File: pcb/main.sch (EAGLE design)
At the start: 45 parts, among them IC1 FT230XS, J3 455-1750-1-ND, J6 M1 connector, J7 M2 connector, Q1 2.5A/30V/105mΩ, U1 LSM303C, U2 ESP-WROOM-32

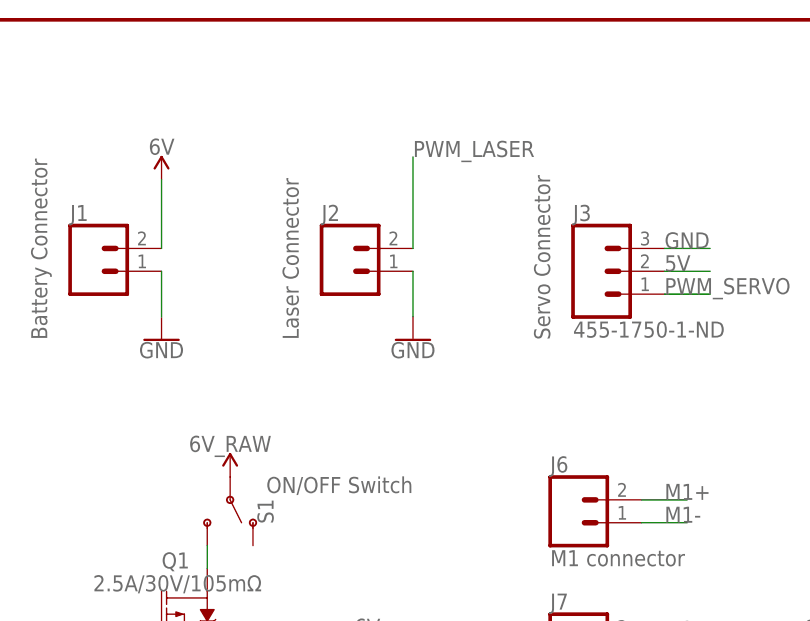
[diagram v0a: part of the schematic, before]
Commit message: mosfet for laser
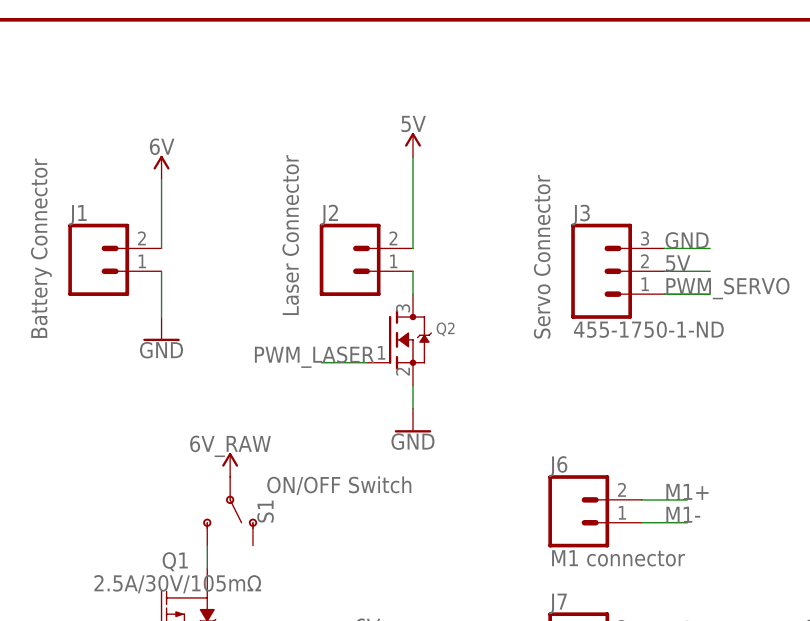
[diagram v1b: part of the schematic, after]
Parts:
- added Q2: (no value), adafruit:MOSFET-NREFLOW
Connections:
- new net N$10: J2.1, Q2.D
- net 5V: now also J2.2
- net GND: now also Q2.S; no longer J2.1
- net PWM_LASER: now also Q2.G; no longer J2.2
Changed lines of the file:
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@@
 <part name="SUPPLY14" library="SparkFun-PowerSymbols" deviceset="VCC" device="" value="3V3"/>
 <part name="RESET" library="DiscreteComponents" deviceset="SWITCH" device="" value=""/>
+<part name="Q2" library="adafruit" library_urn="urn:adsk.eagle:library:420" deviceset="MOSFET-N" device="REFLOW"/>
+<part name="SUPPLY15" library="SparkFun-PowerSymbols" deviceset="VCC" device="" value="5V"/>
 </parts>
 <sheets>
@@
 </instance>
 <instance part="J2" gate="G$1" x="45.72" y="157.48">
-<attribute name="COMM" x="40.64" y="149.86" size="1.778" layer="96" rot="R90"/>
+<attribute name="COMM" x="40.64" y="152.4" size="1.778" layer="96" rot="R90"/>
 </instance>
 <instance part="J3" gate="J$1" x="73.66" y="157.48">
@@
 <instance part="GND1" gate="1" x="142.24" y="152.4"/>
 <instance part="GND2" gate="1" x="116.84" y="152.4"/>
-<instance part="GND3" gate="1" x="53.34" y="149.86"/>
+<instance part="GND3" gate="1" x="53.34" y="139.7"/>
 <instance part="GND4" gate="1" x="25.4" y="149.86"/>
 <instance part="GND5" gate="1" x="38.1" y="45.72"/>
@@
 <instance part="SUPPLY14" gate="G$1" x="172.72" y="124.46"/>
 <instance part="RESET" gate="G$1" x="228.6" y="129.54"/>
+<instance part="Q2" gate="G$1" x="50.8" y="149.86"/>
+<instance part="SUPPLY15" gate="G$1" x="53.34" y="170.18"/>
 </instances>
 <busses>
@@
 <net name="PWM_LASER" class="0">
 <segment>
-<pinref part="J2" gate="G$1" pin="2"/>
-<wire x1="53.34" y1="160.02" x2="53.34" y2="170.18" width="0.1524" layer="91"/>
-<label x="53.34" y="170.18" size="1.778" layer="95"/>
+<pinref part="Q2" gate="G$1" pin="G"/>
+<wire x1="48.26" y1="147.32" x2="43.18" y2="147.32" width="0.1524" layer="91"/>
+<label x="35.56" y="147.32" size="1.778" layer="95"/>
 </segment>
 </net>
@@
 <wire x1="25.4" y1="157.48" x2="25.4" y2="152.4" width="0.1524" layer="91"/>
 <pinref part="GND4" gate="1" pin="GND"/>
-</segment>
-<segment>
-<wire x1="53.34" y1="157.48" x2="53.34" y2="152.4" width="0.1524" layer="91"/>
-<pinref part="J2" gate="G$1" pin="1"/>
-<pinref part="GND3" gate="1" pin="GND"/>
 </segment>
 <segment>
@@
 <pinref part="GND18" gate="1" pin="GND"/>
 </segment>
+<segment>
+<pinref part="Q2" gate="G$1" pin="S"/>
+<pinref part="GND3" gate="1" pin="GND"/>
+<wire x1="53.34" y1="144.78" x2="53.34" y2="142.24" width="0.1524" layer="91"/>
+</segment>
 </net>
 <net name="5V" class="0">
@@
 <junction x="55.88" y="63.5"/>
 <pinref part="U$1" gate="G$1" pin="OUTPUT"/>
+</segment>
+<segment>
+<pinref part="J2" gate="G$1" pin="2"/>
+<wire x1="53.34" y1="160.02" x2="53.34" y2="170.18" width="0.1524" layer="91"/>
+<pinref part="SUPPLY15" gate="G$1" pin="VCC"/>
 </segment>
 </net>
@@
 </segment>
 </net>
+<net name="N$10" class="0">
+<segment>
+<pinref part="Q2" gate="G$1" pin="D"/>
+<pinref part="J2" gate="G$1" pin="1"/>
+<wire x1="53.34" y1="154.94" x2="53.34" y2="157.48" width="0.1524" layer="91"/>
+</segment>
+</net>

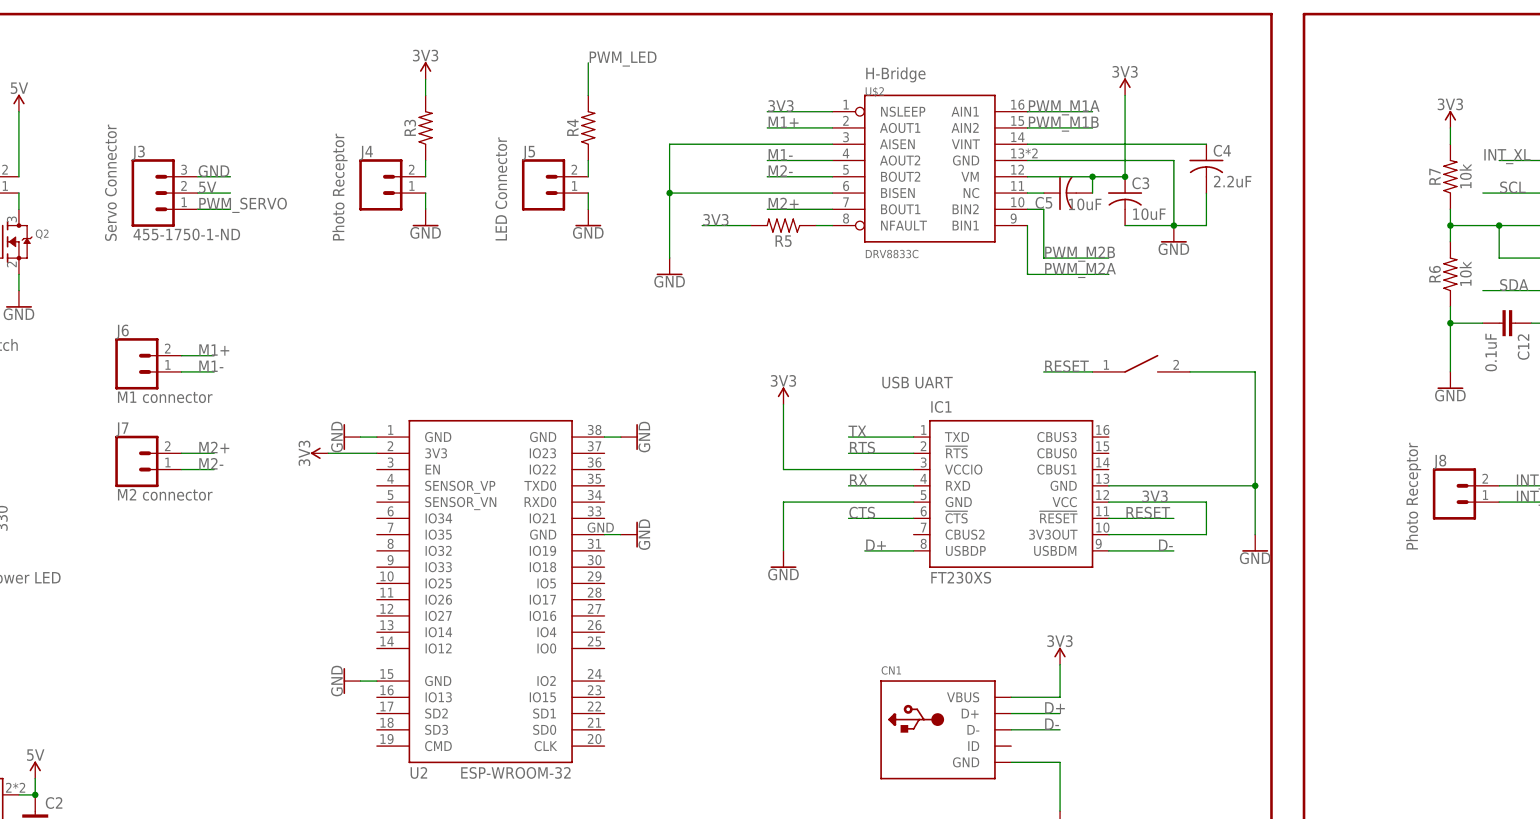
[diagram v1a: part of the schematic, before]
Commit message: wired up almost all of esp's peripherals
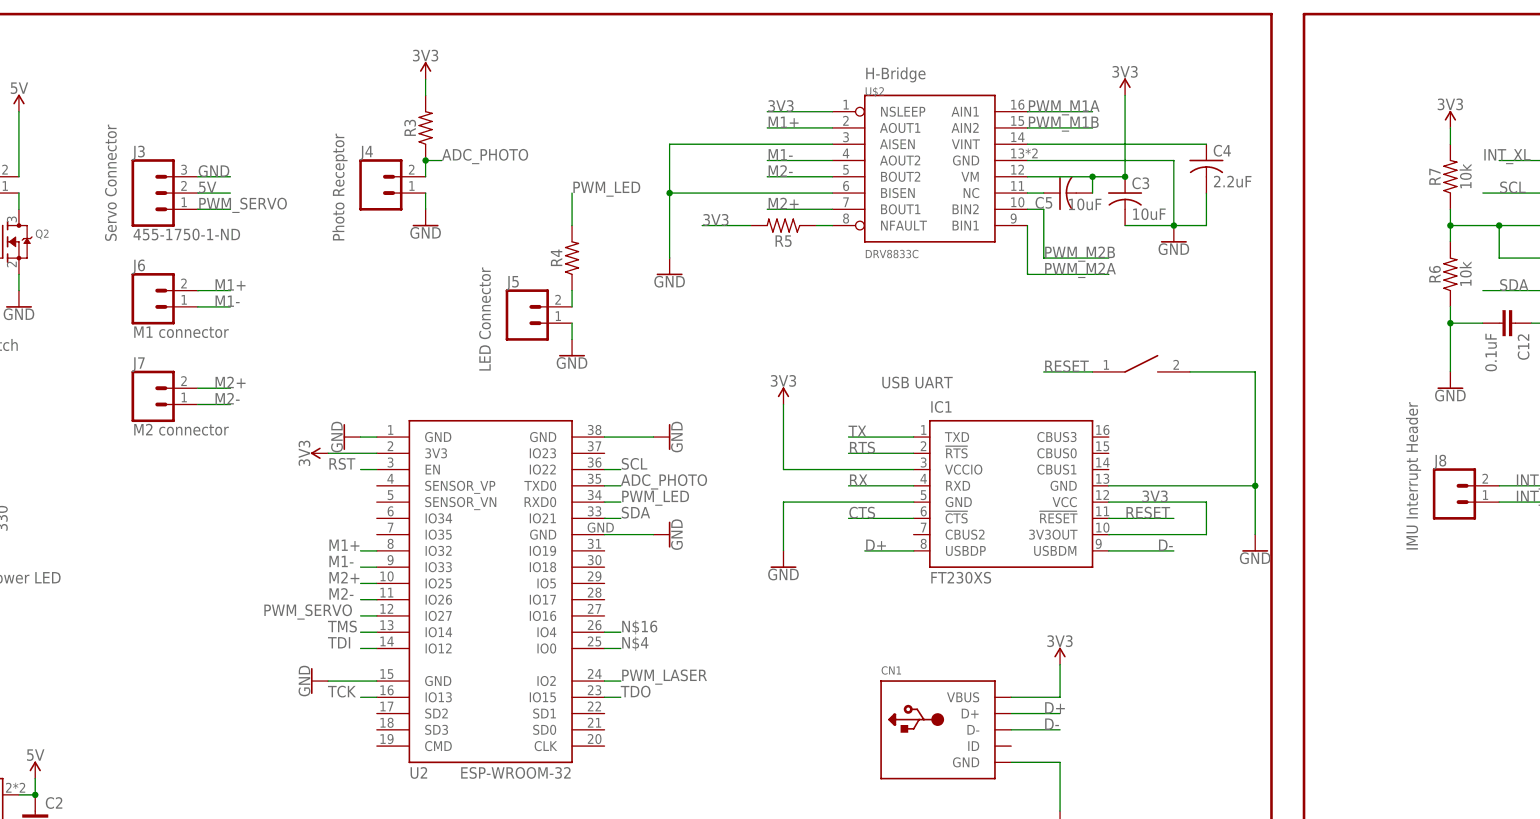
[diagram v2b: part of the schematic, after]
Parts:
- J8: COMM Photo Receptor -> IMU Interrupt Header
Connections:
- new net ADC_PHOTO: J4.2, R3.1, U2.TXD0
- new net N$16: U2.IO4
- new net RST: U2.EN
- new net TCK: U2.IO13
- new net TDI: U2.IO12
- new net TDO: U2.IO15
- new net TMS: U2.IO14
- net M1+: now also U2.IO32
- net M1-: now also U2.IO33
- net M2+: now also U2.IO25
- net M2-: now also U2.IO26
- net N$4: now also U2.IO0; no longer J4.2, R3.1
- net PWM_LASER: now also U2.IO2
- net PWM_LED: now also U2.RXD0
- net PWM_SERVO: now also U2.IO27
- net SCL: now also U2.IO22
- net SDA: now also U2.IO21
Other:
- moved on the sheet: J5, J6, J7, R4

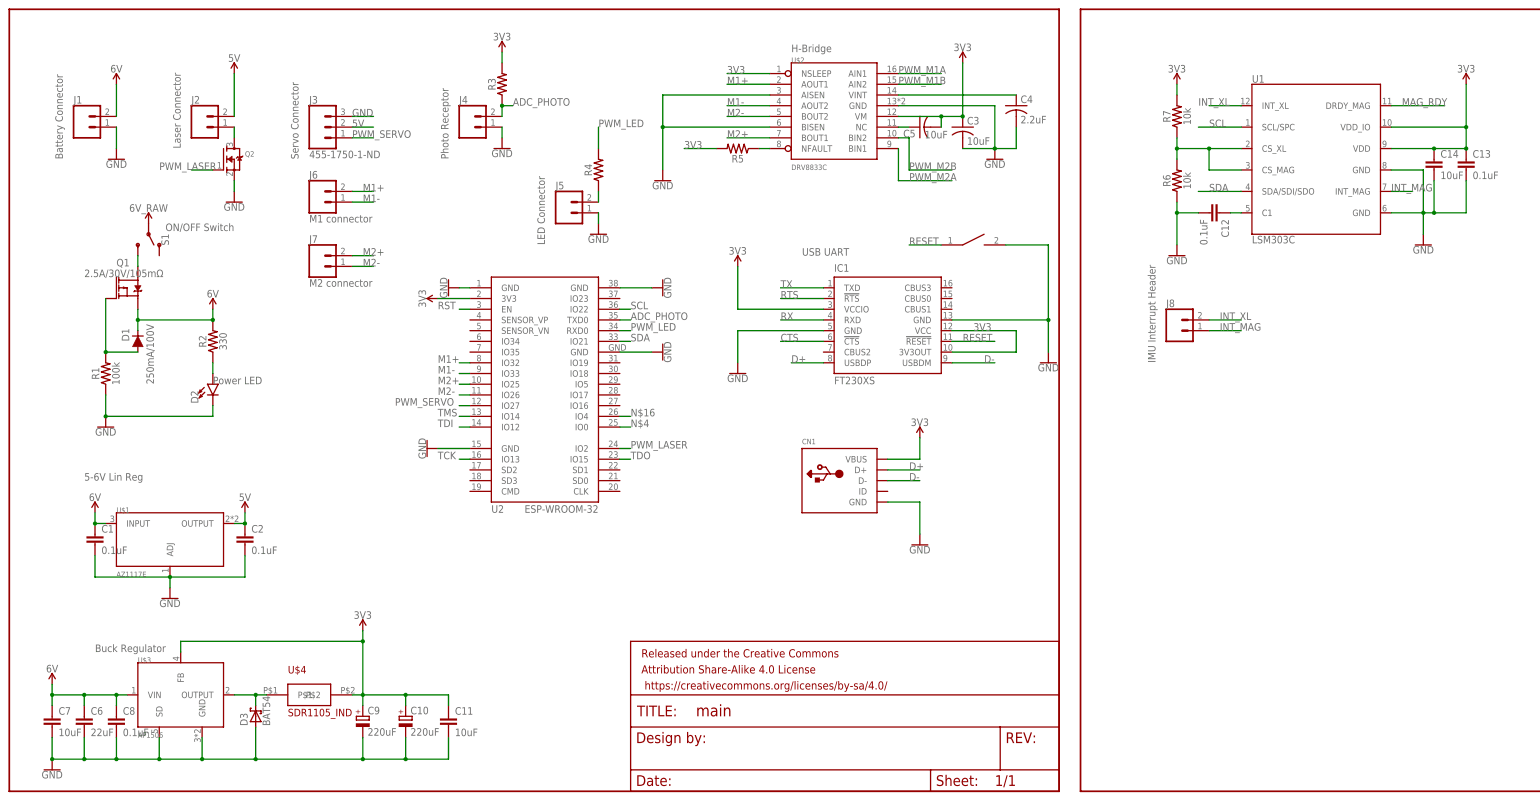
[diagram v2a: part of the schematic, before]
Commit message: more esp pins and isolating grounds
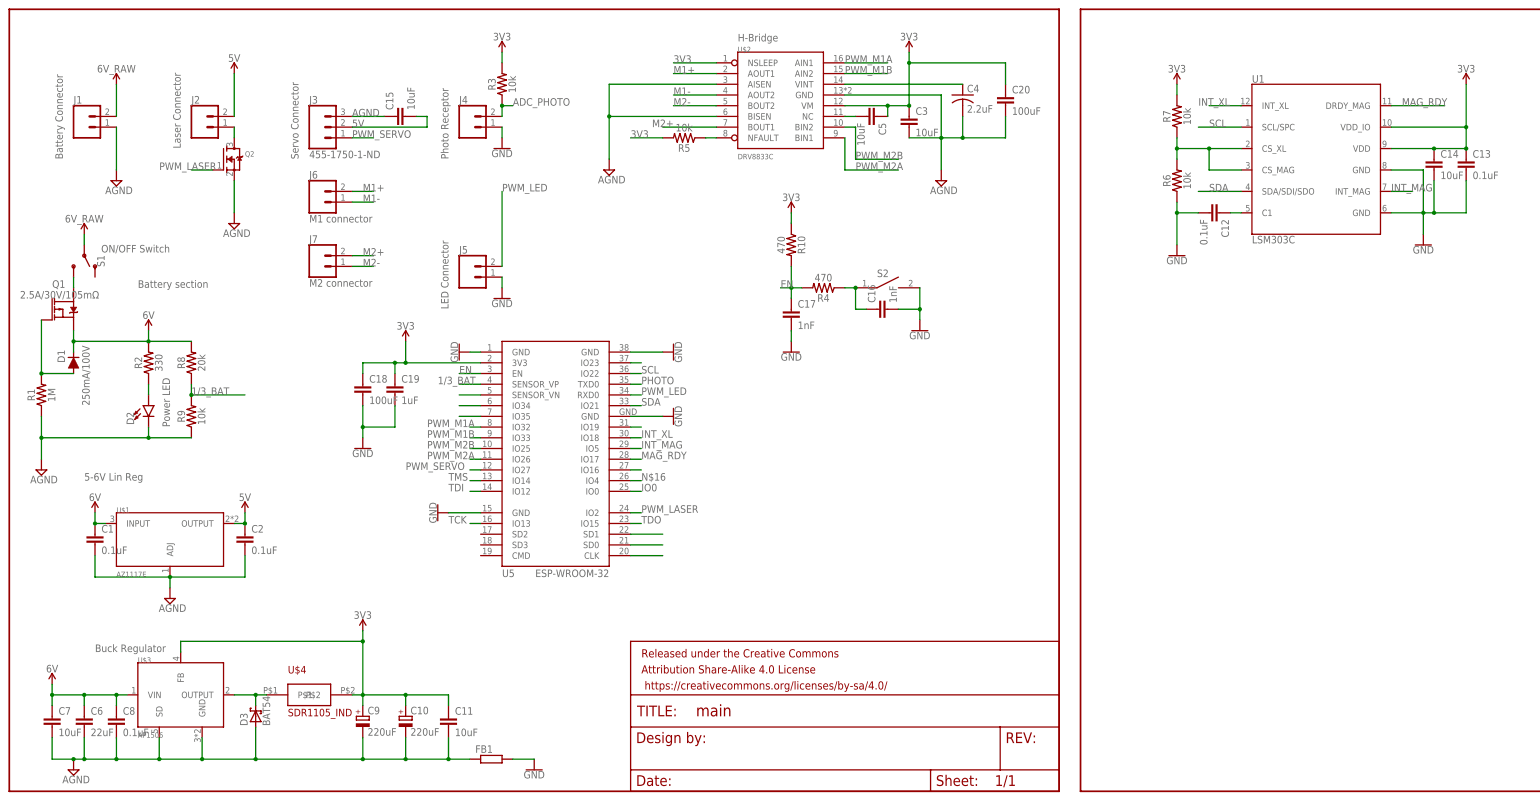
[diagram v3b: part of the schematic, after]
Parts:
- removed CN1: (no value), adafruit:USBMINIB
- removed IC1: FT230XS, electricSheepParty:FT230XS
- removed J8: (no value), electricSheepParty:CONN_02
- removed RESET: SWITCH, DiscreteComponents:SWITCH
- removed U2: ESP-WROOM-32, electricSheepParty:ESP-WROOM-32
- added C15: 10uF, rcl:C-EUC0805
- added C16, C17: 1nF, electricSheepParty:0.1UF-0603-25V-(+80/-20%)
- added C18, C20: 100uF, eagle-ltspice:CC1206
- added C19: 1uF, electricSheepParty:0.1UF-0603-25V-(+80/-20%)
- added FB1: (no value), rcl:R-EU_R0603
- added R10: 470, electricSheepParty:RESISTOR0603
- added R8: 20k, electricSheepParty:RESISTOR0603
- added R9: 10k, electricSheepParty:RESISTOR0603
- added RESET1: S2, DiscreteComponents:SWITCH
- added U5: ESP-WROOM-32, electricSheepParty:ESP-WROOM-32
- C14: device electricSheepParty:0.1UF-0603-25V-(+80/-20%) -> rcl:C-EUC0805
- C3, C5: device rcl:C-USC0603 -> rcl:C-EUC0805
- R1: value 100k -> 1M
- R3, R5: value (none) -> 10k
- R4: value (none) -> 470
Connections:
- removed net CTS: IC1.!CTS
- removed net D+: CN1.D+, IC1.USBDP
- removed net D-: CN1.D-, IC1.USBDM
- removed net RESET: IC1.!RESET, RESET.P$1
- removed net RST: U2.EN
- removed net RTS: IC1.!RTS
- removed net RX: IC1.RXD
- removed net TX: IC1.TXD
- new net 1/3_BAT: R8.1, R9.2, U5.SENSOR_VP
- new net 6V_RAW: J1.2, S1.P
- new net AGND: C1.2, C10.-, C11.2, C15.1, C2.2, C20.2, C3.2, C4.2, C6.2, C7.2, C8.2, C9.-, D2.C, D3.A, FB1.1, J1.1, J3.3, Q2.S, R1.1, R9.1, U$1.ADJ, U$2.AISEN, U$2.BISEN, U$2.GND, U$3.GND, U$3.SD
- new net EN: C17.1, R10.2, R4.2, U5.EN
- new net IO0: U5.IO0
- new net N$11: C16.1, R4.1, RESET1.P$1
- new net N$14: U5.IO35
- new net N$15: U5.CLK
- new net N$17: U5.SD0
- new net N$18: U5.SD1
- new net N$19: U5.IO16
- new net N$23: U5.IO19
- new net N$24: U5.IO23
- new net PHOTO: U5.TXD0
- net 3V3: now also C20.1, C5.1, R10.1; no longer C5.2, CN1.VBUS, IC1.3V3OUT, IC1.VCC, IC1.VCCIO, U2.3V3
- net 5V: now also C15.2
- net 6V: now also D1.C, Q1.S, R2.2, R8.2
- net ADC_PHOTO: no longer U2.TXD0
- net GND: now also C16.2, C17.2, C18.2, C19.2, FB1.2, RESET1.P$2, U5.GND@1, U5.GND@2, U5.GND@3, U5.GND@4; no longer C1.2, C10.-, C11.2, C2.2, C3.2, C4.2, C6.2, C7.2, C8.2, C9.-, CN1.GND, D2.C, D3.A, IC1.GND, IC1.GND@1, J1.1, J3.3, Q2.S, R1.1, RESET.P$2, U$1.ADJ, U$2.AISEN, U$2.BISEN, U$2.GND, U$3.GND, U$3.SD, U2.GND@1, U2.GND@2, U2.GND@3, U2.GND@4
- net INT_MAG: now also U5.IO5; no longer J8.1
- net INT_XL: now also U5.IO18; no longer J8.2
- net M1+: no longer U2.IO32
- net M1-: no longer U2.IO33
- net M2+: no longer U2.IO25
- net M2-: no longer U2.IO26
- net MAG_RDY: now also U5.IO17
- net N$16: now also U5.IO4; no longer U2.IO4
- net N$4: now also U5.SENSOR_VN; no longer U2.IO0
- net N$5: now also U5.IO34; no longer J5.2, R4.1
- net N$9: now also C5.2; no longer C5.1
- net PWM_LASER: now also U5.IO2; no longer U2.IO2
- net PWM_LED: now also J5.2, U5.RXD0; no longer R4.2, U2.RXD0
- net PWM_M1A: now also U5.IO32
- net PWM_M1B: now also U5.IO33
- net PWM_M2A: now also U5.IO26
- net PWM_M2B: now also U5.IO25
- net PWM_SERVO: now also U5.IO27; no longer U2.IO27
- net SCL: now also U5.IO22; no longer U2.IO22
- net SDA: now also U5.IO21; no longer U2.IO21
- net TCK: now also U5.IO13; no longer U2.IO13
- net TDI: now also U5.IO12; no longer U2.IO12
- net TDO: now also U5.IO15; no longer U2.IO15
- net TMS: now also U5.IO14; no longer U2.IO14
- net VCC: now also C18.1, C19.1, U5.3V3; no longer D1.C, J1.2, Q1.S, R2.2, S1.P
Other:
- note added: "Battery section"
- note added: "S2"
- moved on the sheet: C3, C4, C5, D1, D2, J5, Q1, R1, R2, R4, R5, S1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
